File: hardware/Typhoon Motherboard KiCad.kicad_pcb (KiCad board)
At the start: 2 copper layers, 73.5 x 52.8 mm, 61 parts, among them J1 Conn_01x04_Pin, J10 USB_C_Receptacle_USB2.0, J11 Conn_01x02_Pin, J12 Conn_01x02_Pin, J13 Conn_01x02_Pin, J14 Conn_01x02_Pin, J15 Conn_01x02_Pin, J16 Conn_01x02_Pin, J2 Conn_02x03_Odd_Even, J3 Conn_01x04_Pin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

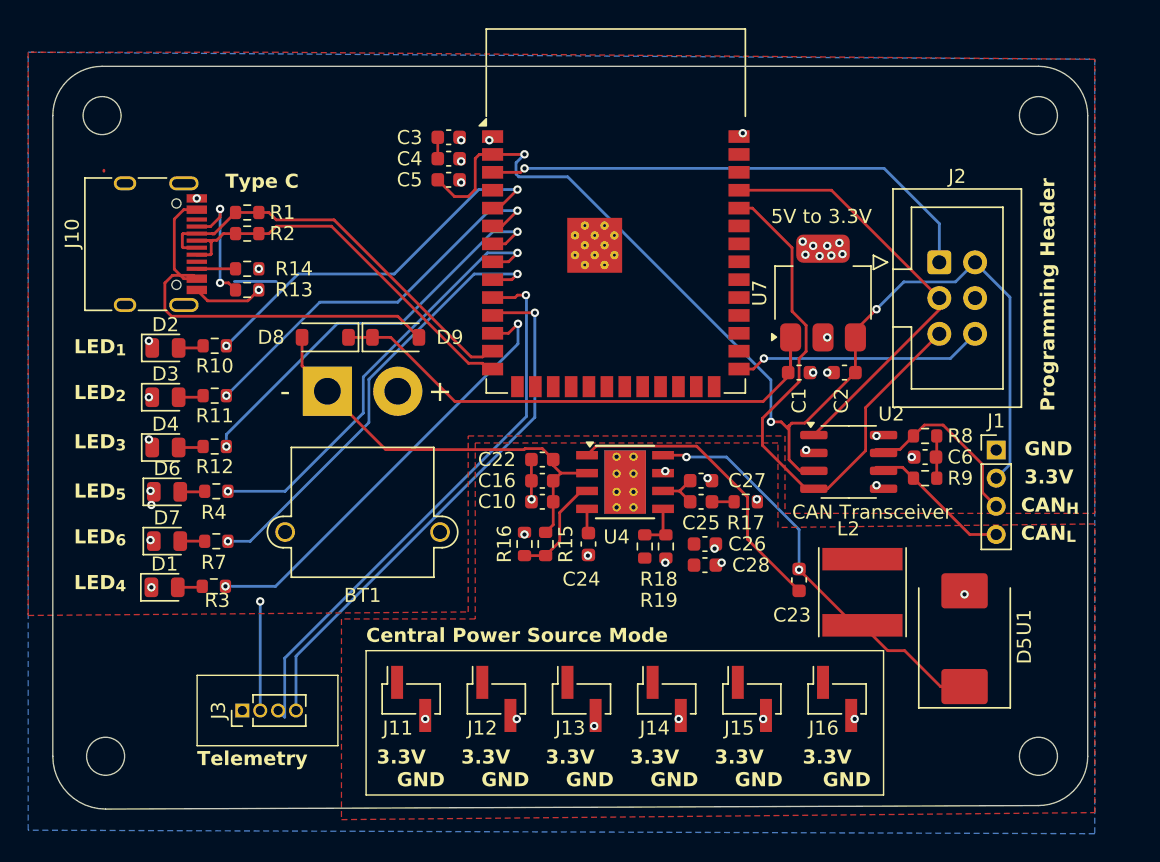
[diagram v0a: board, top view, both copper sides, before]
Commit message: Updated the Boost Converter
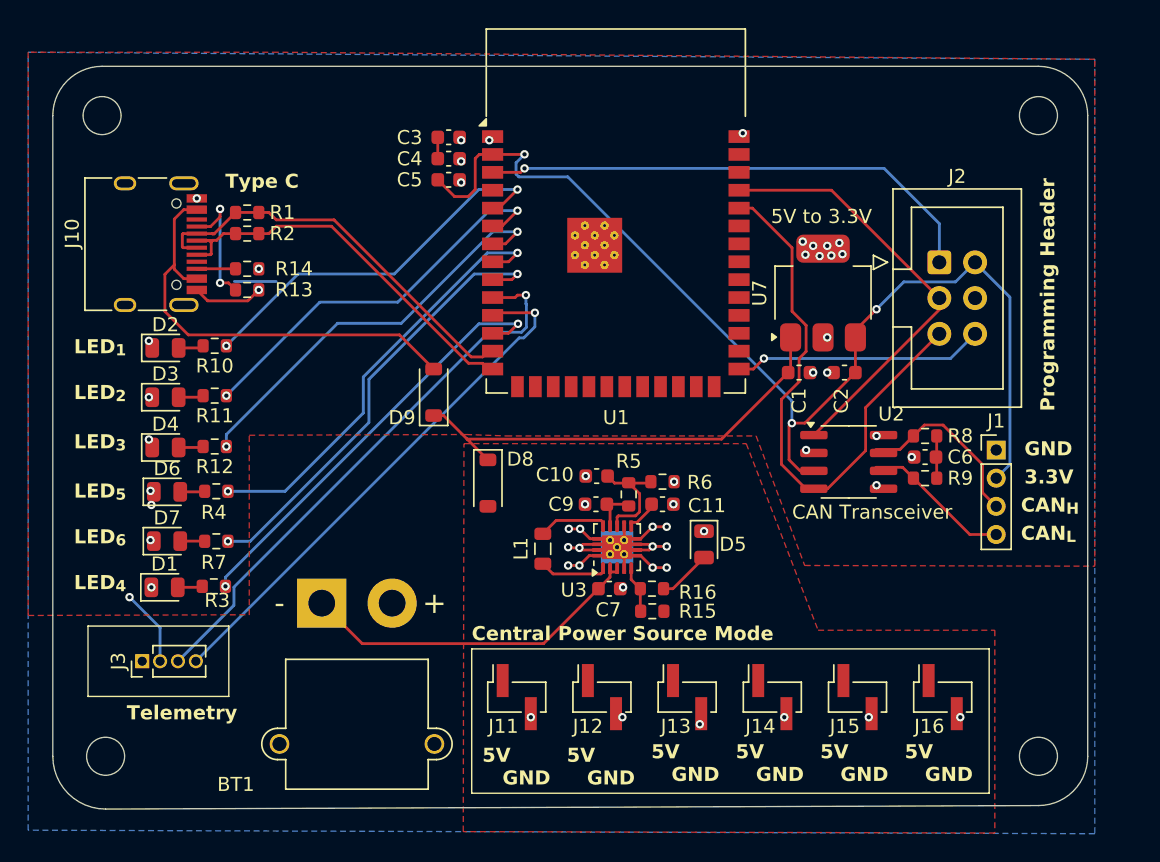
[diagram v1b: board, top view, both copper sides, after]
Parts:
- removed C16, C22: 4.7u, Capacitor_SMD:C_0603_1608Metric
- removed C23: 0.1u, Capacitor_SMD:C_0603_1608Metric
- removed C24: 0.01u, Capacitor_SMD:C_0603_1608Metric
- removed C25: 1000p, Capacitor_SMD:C_0603_1608Metric
- removed C26, C27, C28: 47u, Capacitor_SMD:C_0603_1608Metric
- removed L2: 4.7u, Inductor_SMD:L_Taiyo-Yuden_NR-60xx
- removed R17: 29.4k, Resistor_SMD:R_0603_1608Metric
- removed R18: 10.2k, Resistor_SMD:R_0603_1608Metric
- removed R19: 3.24k, Resistor_SMD:R_0603_1608Metric
- removed U4: TPS54331DDA, Package_SO:TI_SO-PowerPAD-8_ThermalVias
- added C11: 0.1 uF, Capacitor_SMD:C_0603_1608Metric, F.Cu at (144.8, 106.8)
- added C7: 20uF, Capacitor_SMD:C_0603_1608Metric, F.Cu at (141.0, 112.8)
- added C9: 66uF, Capacitor_SMD:C_0603_1608Metric, F.Cu at (140.1, 106.8)
- added L1: 1 uH, Inductor_SMD:L_0805_2012Metric, F.Cu at (136.3, 110.0)
- added R5: 1M, Resistor_SMD:R_0603_1608Metric, F.Cu at (142.4, 106.2)
- added R6: 111k, Resistor_SMD:R_0603_1608Metric, F.Cu at (144.8, 105.2)
- added U3: TPS63060, Package_SON:Texas_S-PWSON-N10_ThermalVias, F.Cu at (141.6, 109.9)
- C10: value 4.7u -> 10pF
- D5: value B340 -> LED; footprint Diode_SMD:D_SMC -> LED_SMD:LED_0805_2012Metric
- R15: value 200k -> 1M
- R16: value 98k -> 330
- moved D5 19.7 mm to (147.8, 109.7), turned to -90 degrees
- moved D8 15.5 mm to (132.4, 105.3), turned to -90 degrees
- moved BT1 15.1 mm to (120.6, 113.9)
- moved R16 9.59 mm to (144.1, 112.8), turned to 0 degrees
- moved R15 8.95 mm to (144.1, 114.5), turned to 180 degrees
- moved J3 7.92 mm to (107.8, 118.0)
- moved J12 7.50 mm to (140.5, 120.5)
- moved J13 7.50 mm to (146.6, 120.5)
- moved J14 7.50 mm to (152.6, 120.5)
- moved J15 7.50 mm to (158.7, 120.5)
- moved J16 7.50 mm to (164.7, 120.5)
- moved J11 7.50 mm to (134.4, 120.5)
- moved D9 4.74 mm to (128.6, 98.9), turned to 90 degrees
- moved C10 4.27 mm to (140.1, 104.8)
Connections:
- net Net-(U4-EN) renamed /CentralPowerSource/PG
- C10 pad 1: +BATT -> Net-(U3-FB)
- D5 pad 1: Net-(D5-K) -> GND
- D5 pad 2: GND -> Net-(D5-A)
- D8 pad 2: +BATT -> +5VA
- J11 pad 1: +3.3VA -> +5VA
- J12 pad 1: +3.3VA -> +5VA
- J13 pad 1: +3.3VA -> +5VA
- J14 pad 1: +3.3VA -> +5VA
- J15 pad 1: +3.3VA -> +5VA
- J16 pad 1: +3.3VA -> +5VA
- R15 pad 1: +BATT -> +5VA
- R16 pad 2: GND -> Net-(D5-A)
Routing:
- net Net-(D5-K): track 29.9 -> 0.00 mm, vias 2 -> 0
- net Net-(U4-BOOT): track 21.3 -> 0.00 mm
- net GND: track 11.0 -> 26.4 mm, vias 46 -> 54
- net Net-(U3-FB): track 0.00 -> 7.84 mm
- net +5V: track 39.3 -> 32.5 mm
- net +BATT: track 30.4 -> 24.5 mm
- net Net-(U3-L2): track 0.00 -> 4.73 mm
- net Net-(U3-L1): track 0.00 -> 4.63 mm
- net /CentralPowerSource/PG: track 7.55 -> 3.07 mm
- net Net-(D5-A): track 0.00 -> 3.79 mm
- net /CentralPowerSource/VSENSE: track 3.43 -> 0.00 mm
- net +3.3V: track 90.0 -> 86.7 mm
- net Net-(U4-COMP): track 3.30 -> 0.00 mm
- net +5VA: track 0.00 -> 2.98 mm
- net Net-(U3-VAUX): track 0.00 -> 2.13 mm
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- added copper zone on F.Cu, net +5VA
- removed copper zone on F.Cu, net +3.3VA
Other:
- board text added: "5V GND"
- board text removed: "3.3V GND"

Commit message: Production Files
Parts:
- D8, D9: value D -> D_Schottky
- R1, R2: value 22R -> 22
- moved D8 7.67 mm to (128.5, 98.8), turned to 90 degrees
- moved D9 7.35 mm to (132.2, 105.2), turned to -90 degrees
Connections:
- C7 pad 1: +BATT -> unconnected-(C7-Pad1)
- C7 pad 2: GND -> unconnected-(C7-Pad2)
- D8 pad 2: +5VA -> VDC
- D9 pad 2: VDC -> +5VA
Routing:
- net unconnected-(C7-Pad2): vias 0 -> 1
- net GND: vias 54 -> 53
